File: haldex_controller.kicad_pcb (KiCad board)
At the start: 2 copper layers, 41 x 10.8 mm, 219 parts, among them IC1 TPS62A02DRLR, IC2 TPS2553DBVT, IC3 LBEE5KL1YN-814, IC4 TLIN1027DRQ1, J1 GND, J10 12V in, J11 K Line, J12 Brake Light, J13 Handbrake, J2 BOOT0, J3 JTAG, J4 Debug, J5 USB, J6 Conn_Coaxial_Small, J7 Body 120R, J8 Hldx 120R, J9 ECU Connector, Q1 STR1550, Q2 BC807, Q3 Si7119DN, SW1 ~{RST}, SW2 Config, U1 LMR33630BDDA, U10 G3VM-61VY2, U11 G3VM-61VY2, U12 G3VM-61VY2, U13 G3VM-61VY2, U14 G3VM-61VY2, U15 G3VM-61VY2, U16 G3VM-61VY2, U17 G3VM-61VY2, U2 STM32H573VITx, U3 PCA9557PW, U4 SST25VF080B-50-4x-S2Ax, U5 APS6404L-3SQR-SN, U6 USBLC6-2SC6, U8 TJA1051T-3, U9 TJA1051T-3, X1 32.768kHz, Y1 25MHz

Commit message: working on component placement
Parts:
- moved H3 265.3 mm to (158.8, 138.4)
- moved H2 261.5 mm to (157.5, 47.6)
- moved R4 258.1 mm to (159.7, 119.9)
- moved R3 255.1 mm to (155.9, 122.4)
- moved R5 254.7 mm to (160.0, 111.1)
- moved R6 253.8 mm to (160.0, 108.0), turned to 180 degrees
- moved R7 252.8 mm to (161.3, 84.7), turned to 90 degrees
- moved C9 252.1 mm to (156.2, 86.0)
- moved C2 252.0 mm to (156.2, 100.6)
- moved C7 251.7 mm to (156.2, 89.8)
- moved J10 249.7 mm to (158.1, 129.5), turned to 90 degrees
- moved R13 248.7 mm to (160.7, 97.4), turned to 90 degrees
- moved R12 248.5 mm to (160.7, 93.0), turned to 90 degrees
- moved Q2 245.8 mm to (154.8, 111.1)
- moved R8 243.5 mm to (149.9, 111.1), turned to -90 degrees
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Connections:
- D10 pad 1: GND -> Net-(D10-K)
- D10 pad 2: Net-(D10-A) -> /MCU/LED_HLDX_ERR
- D11 pad 1: GND -> Net-(D11-K)
- D11 pad 2: Net-(D11-A) -> /MCU/LED0
- D12 pad 1: GND -> Net-(D12-K)
- D12 pad 2: Net-(D12-A) -> /MCU/LED1
- D5 pad 1: GND -> Net-(D5-K)
- D5 pad 2: Net-(D5-A) -> /MCU/LED_BODY_TX
- D6 pad 1: GND -> Net-(D6-K)
- D6 pad 2: Net-(D6-A) -> /MCU/LED_BODY_RX
- D7 pad 1: GND -> Net-(D7-K)
- D7 pad 2: Net-(D7-A) -> /MCU/LED_BODY_ERR
- D8 pad 1: GND -> Net-(D8-K)
- D8 pad 2: Net-(D8-A) -> /MCU/LED_HLDX_TX
- D9 pad 1: GND -> Net-(D9-K)
- D9 pad 2: Net-(D9-A) -> /MCU/LED_HLDX_RX
- L7 pad 1: Net-(U8-CANH) -> Net-(U8-CANL)
- L7 pad 2: Net-(U8-CANL) -> /CAN PHYs/BODY_CAN_L
- L7 pad 4: /CAN PHYs/BODY_CAN_L -> Net-(U8-CANH)
- L8 pad 1: Net-(U9-CANH) -> Net-(U9-CANL)
- L8 pad 2: Net-(U9-CANL) -> /CAN PHYs/HLDX_CAN_L
- L8 pad 4: /CAN PHYs/HLDX_CAN_L -> Net-(U9-CANH)
- R30 pad 1: /MCU/LED_BODY_TX -> Net-(D5-K)
- R30 pad 2: Net-(D5-A) -> GND
- R31 pad 1: /MCU/LED_BODY_RX -> Net-(D6-K)
- R31 pad 2: Net-(D6-A) -> GND
- R32 pad 1: /MCU/LED_BODY_ERR -> Net-(D7-K)
- R32 pad 2: Net-(D7-A) -> GND
- R33 pad 1: /MCU/LED_HLDX_TX -> Net-(D8-K)
- R33 pad 2: Net-(D8-A) -> GND
- R34 pad 1: /MCU/LED_HLDX_RX -> Net-(D9-K)
- R34 pad 2: Net-(D9-A) -> GND
- R35 pad 1: /MCU/LED_HLDX_ERR -> Net-(D10-K)
- R35 pad 2: Net-(D10-A) -> GND
- R36 pad 1: /MCU/LED0 -> Net-(D11-K)
- R36 pad 2: Net-(D11-A) -> GND
- R37 pad 1: /MCU/LED1 -> Net-(D12-K)
- R37 pad 2: Net-(D12-A) -> GND
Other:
- board size 41 x 10.8 mm -> 68 x 100 mm
- copper layers 2 -> 4

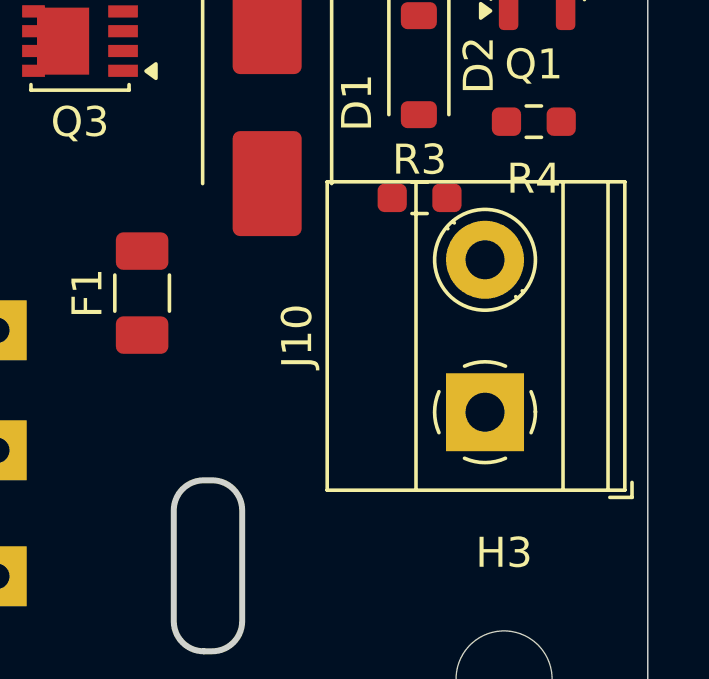
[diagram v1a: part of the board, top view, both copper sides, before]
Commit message: sch: J10 footprint update
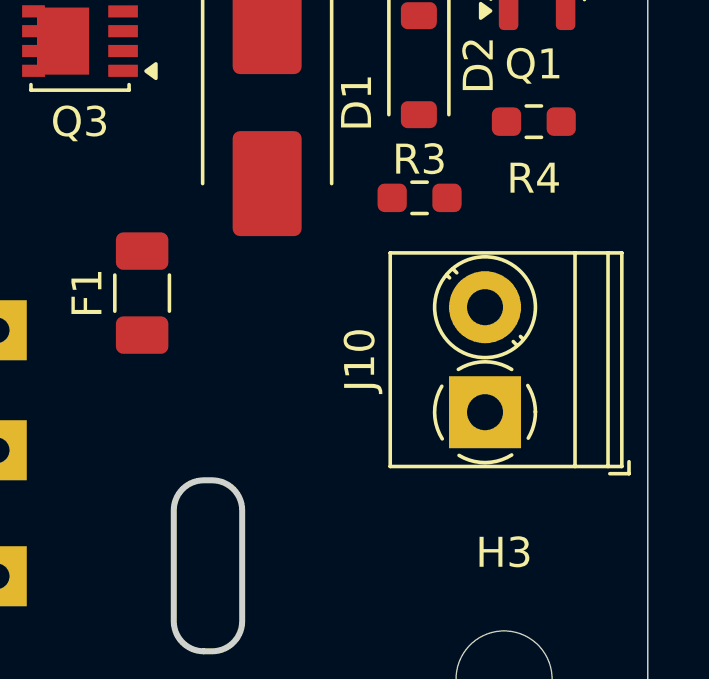
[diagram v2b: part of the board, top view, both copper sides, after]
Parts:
- J10: footprint TerminalBlock_Phoenix:TerminalBlock_Phoenix_MKDS-1,5-2-5.08_1x02_P5.08mm_Horizontal -> TerminalBlock_Phoenix:TerminalBlock_Phoenix_PT-1,5-2-3.5-H_1x02_P3.50mm_Horizontal

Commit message: brd: routing in progress
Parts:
- removed ANT1: W3000, W3000:W3000
- removed F2: 500mA, Fuse:Fuse_1206_3216Metric
- removed FB5, FB8: FerriteBead_Small, Inductor_SMD:L_0805_2012Metric_Pad1.05x1.20mm_HandSolder
- removed R48, R50: 0, Resistor_SMD:R_0402_1005Metric_Pad0.72x0.64mm_HandSolder
- removed TP10: SDIO_CMD, TestPoint:TestPoint_Pad_D1.0mm
- removed TP11: SDIO_DATA_2, TestPoint:TestPoint_Pad_D1.0mm
- removed TP12: SDIO_CLK, TestPoint:TestPoint_Pad_D1.0mm
- removed TP14: SDIO_DATA_0, TestPoint:TestPoint_Pad_D1.0mm
- removed TP15: SDIO_DATA_3, TestPoint:TestPoint_Pad_D1.0mm
- removed TP16: SDIO_DATA_1, TestPoint:TestPoint_Pad_D1.0mm
- added AE1: type1YN-antenna-p2ml4452-1, 1yn_antenna:1YN_ANTENNA, F.Cu at (98.4, 52.4)
- added C48: 4p7, Capacitor_SMD:C_0402_1005Metric_Pad0.74x0.62mm_HandSolder, F.Cu at (99.1, 63.3)
- added C49: 4p7, Capacitor_SMD:C_0402_1005Metric_Pad0.74x0.62mm_HandSolder, F.Cu at (99.1, 57.8)
- added C50: 100n, Capacitor_SMD:C_0603_1608Metric_Pad1.08x0.95mm_HandSolder, F.Cu at (133.9, 87.8)
- added C51: 100n, Capacitor_SMD:C_0603_1608Metric_Pad1.08x0.95mm_HandSolder, B.Cu at (154.7, 106.4)
- added L9: LQW15AN2N4B00D, Inductor_SMD:L_0402_1005Metric, F.Cu at (98.5, 52.8)
- added TP3: V_{BUS}, TestPoint:TestPoint_Pad_D1.0mm, F.Cu at (128.7, 54.2)
- C11, C12, C24, C31, C35, C37, C38, C39, C40, C41, C42, C43, C44, C45, C46, C47, D13, D14, D16, D17, D18, D19, F3, IC4, L4, L7, L8, R14, R18, R20, R25, R26, R27, R28, R30, R31, R32, R33, R34, R35, R36, R37, R51, R52, R53, R54, R69, R70, R71, TP13, U3, U8, U9, X1, Y1: moved to B.Cu
- J2: footprint Connector_PinHeader_2.54mm:PinHeader_1x02_P2.54mm_Vertical -> Connector_PinHeader_1.27mm:PinHeader_1x02_P1.27mm_Vertical
- J6: value Conn_Coaxial_Small -> MM8130-2600RA2; footprint Connector_Coaxial:U.FL_Molex_MCRF_73412-0110_Vertical -> MM8130-2600RA2:MM81302600RA2
- R42, R43, R44, R45, R46: footprint Resistor_SMD:R_0603_1608Metric_Pad0.98x0.95mm_HandSolder -> Resistor_SMD:R_0402_1005Metric_Pad0.72x0.64mm_HandSolder
- U4: footprint Package_SO:SOIC-8_5.275x5.275mm_P1.27mm -> Package_SO:SOIC-8_3.9x4.9mm_P1.27mm
- moved D4 372.5 mm to (144.0, 111.9), turned to -90 degrees
- moved R14 369.1 mm to (141.0, 114.0)
- moved L4 353.5 mm to (161.2, 108.8), turned to 90 degrees
- moved R27 305.2 mm to (148.1, 64.9), turned to 90 degrees
- moved C24 297.0 mm to (143.9, 65.0)
- moved R26 293.5 mm to (136.5, 62.0)
- moved R25 289.8 mm to (136.5, 63.8)
- moved U3 289.2 mm to (143.9, 60.2)
- moved D12 288.1 mm to (159.6, 54.5), turned to 0 degrees
- moved D5 285.8 mm to (159.6, 64.9), turned to 0 degrees
- moved D6 285.8 mm to (159.6, 62.1), turned to 0 degrees
- moved D7 285.7 mm to (159.6, 59.2), turned to 0 degrees
- moved R54 285.2 mm to (113.3, 118.4), turned to 90 degrees
- moved D8 281.0 mm to (152.1, 65.0), turned to 0 degrees
- moved R53 280.9 mm to (109.7, 118.4), turned to -90 degrees
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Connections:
- C33 pad 2: SR_PVSS -> GND
- C34 pad 2: Net-(C34-Pad2) -> Net-(J6-OUT)
- C35 pad 2: SR_PVSS -> GND
- D10 pad 1: Net-(D10-K) -> GND
- D10 pad 2: /MCU/LED_HLDX_ERR -> Net-(D10-A)
- D11 pad 1: Net-(D11-K) -> GND
- D11 pad 2: /MCU/LED0 -> Net-(D11-A)
- D12 pad 1: Net-(D12-K) -> GND
- D12 pad 2: /MCU/LED1 -> Net-(D12-A)
- D20 pad 1: /Connector/USER_INPUT_1 -> /Connector/USER_INPUT_2
- D20 pad 2: /Connector/USER_INPUT_2 -> /Connector/USER_INPUT_1
- D21 pad 1: /Connector/USER_OUTPUT_1 -> /Connector/USER_OUTPUT_2
- D21 pad 2: /Connector/USER_OUTPUT_2 -> /Connector/USER_OUTPUT_1
- D5 pad 1: Net-(D5-K) -> GND
- D5 pad 2: /MCU/LED_BODY_TX -> Net-(D5-A)
- D6 pad 1: Net-(D6-K) -> GND
- D6 pad 2: /MCU/LED_BODY_RX -> Net-(D6-A)
- D7 pad 1: Net-(D7-K) -> GND
- D7 pad 2: /MCU/LED_BODY_ERR -> Net-(D7-A)
- D8 pad 1: Net-(D8-K) -> GND
- D8 pad 2: /MCU/LED_HLDX_TX -> Net-(D8-A)
- D9 pad 1: Net-(D9-K) -> GND
- D9 pad 2: /MCU/LED_HLDX_RX -> Net-(D9-A)
- IC3 pad 32: SR_PVSS -> GND
- IC3 pad 33: SR_PVSS -> GND
- J5 pad A4: Net-(F2-Pad1) -> VBUS
- J5 pad A6: Net-(J5-D+-PadA6) -> /USB/USB_CONN_DP
- J5 pad A7: Net-(J5-D--PadA7) -> /USB/USB_CONN_DN
- J5 pad A9: Net-(F2-Pad1) -> VBUS
- J5 pad B4: Net-(F2-Pad1) -> VBUS
- J5 pad B6: Net-(J5-D+-PadA6) -> /USB/USB_CONN_DP
- J5 pad B7: Net-(J5-D--PadA7) -> /USB/USB_CONN_DN
- J5 pad B9: Net-(F2-Pad1) -> VBUS
- J6 pad 1: Net-(J6-In) -> /WiFi and Bluetooth/ANT_FEED
- J6 pad 2: GND -> Net-(J6-OUT)
- L5 pad 3: /MCU/USB_DN -> /MCU/USB_DP
- L5 pad 4: /MCU/USB_DP -> /MCU/USB_DN
- R30 pad 1: Net-(D5-K) -> /MCU/LED_BODY_TX
- R30 pad 2: GND -> Net-(D5-A)
- R31 pad 1: Net-(D6-K) -> /MCU/LED_BODY_RX
- R31 pad 2: GND -> Net-(D6-A)
- R32 pad 1: Net-(D7-K) -> /MCU/LED_BODY_ERR
- R32 pad 2: GND -> Net-(D7-A)
- R33 pad 1: Net-(D8-K) -> /MCU/LED_HLDX_TX
- R33 pad 2: GND -> Net-(D8-A)
- R34 pad 1: Net-(D9-K) -> /MCU/LED_HLDX_RX
- R34 pad 2: GND -> Net-(D9-A)
- R35 pad 1: Net-(D10-K) -> /MCU/LED_HLDX_ERR
- R35 pad 2: GND -> Net-(D10-A)
- R36 pad 1: Net-(D11-K) -> /MCU/LED0
- R36 pad 2: GND -> Net-(D11-A)
- R37 pad 1: Net-(D12-K) -> /MCU/LED1
- R37 pad 2: GND -> Net-(D12-A)
- R47 pad 1: /WiFi and Bluetooth/ANT_FEED -> Net-(C49-Pad2)
- R47 pad 2: Net-(J6-In) -> Net-(C36-Pad2)
- R49 pad 2: Net-(C34-Pad2) -> Net-(J6-OUT)
- U2 pad 2: unconnected-(U2-PE3-Pad2) -> /CAN PHYs/HLDX_CAN_S
- U2 pad 61: /MCU/DIP_3 -> /MCU/DIP_4
- U2 pad 62: /MCU/DIP_4 -> /MCU/DIP_3
- U2 pad 93: /CAN PHYs/HLDX_CAN_S -> unconnected-(U2-PB7-Pad93)
- U3 pad 10: /MCU/LED_HLDX_TX -> /MCU/LED_HLDX_ERR
- U3 pad 11: /MCU/LED_HLDX_RX -> /MCU/LED_BODY_RX
- U3 pad 12: /MCU/LED_HLDX_ERR -> /MCU/LED_HLDX_RX
- U3 pad 13: /MCU/LED0 -> /MCU/LED_BODY_TX
- U3 pad 14: /MCU/LED1 -> /MCU/LED_HLDX_TX
- U3 pad 6: /MCU/LED_BODY_TX -> /MCU/LED1
- U3 pad 7: /MCU/LED_BODY_RX -> /MCU/LED0
- U6 pad 1: Net-(J5-D--PadA7) -> /USB/USB_CONN_DP
- U6 pad 3: Net-(J5-D+-PadA6) -> /USB/USB_CONN_DN
- U6 pad 5: Net-(U6-VBUS) -> VBUS
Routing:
- net +3V3: track 0.00 -> 89.9 mm, vias 0 -> 17
- net /MCU/MCU_USER_INPUT_1: track 0.00 -> 87.4 mm, vias 0 -> 2
- net /MCU/MCU_BODY_HANDBRAKE: track 0.00 -> 86.0 mm, vias 0 -> 2
- net /MCU/MCU_BODY_BRAKES: track 0.00 -> 83.6 mm, vias 0 -> 2
- net /MCU/MCU_USER_INPUT_2: track 0.00 -> 80.8 mm, vias 0 -> 2
- net /Connector/HLDX_K_LINE: track 0.00 -> 72.5 mm
- net /Connector/USER_INPUT_2: track 0.00 -> 67.9 mm
- net /CAN PHYs/BODY_CAN_S: track 0.00 -> 62.4 mm, vias 0 -> 1
- net /Connector/USER_INPUT_1: track 0.00 -> 62.3 mm
- net /MCU/I2S2_WS: track 0.00 -> 62.0 mm, vias 0 -> 2
- net /MCU/MCU_HLDX_HANDBRAKE: track 0.00 -> 61.3 mm, vias 0 -> 2
- net /MCU/LIN_EN: track 0.00 -> 60.0 mm, vias 0 -> 1
- net /MCU/MCU_HLDX_BRAKES: track 0.00 -> 59.5 mm, vias 0 -> 2
- net /MCU/LIN_TX: track 0.00 -> 58.4 mm, vias 0 -> 1
- net /MCU/JTAG_~{RST}: track 0.00 -> 58.4 mm, vias 0 -> 3
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- added copper zone on F.Cu, net +3V3
- added copper zone on B.Cu, net +BATT
- added copper zone on F.Cu, net +BATT
- added copper zone on B.Cu, net /Connector/USER_BATT
- added copper zone on F.Cu, net /WiFi and Bluetooth/SR_VLX
- added copper zone on F.Cu, net /WiFi and Bluetooth/VIN_LDO
- added copper zone on B.Cu, net GND
- added copper zone on F.Cu, net GND
- added copper zone on In1.Cu, net GND
- added copper zone on B.Cu, net GNDPWR
- added copper zone on F.Cu, net GNDPWR
- added copper zone on F.Cu, net Net-(C10-Pad2)
- added copper zone on F.Cu, net Net-(D1-A)
- added copper zone on F.Cu, net Net-(D1-K)
- added copper zone on F.Cu, net Net-(Q3-D)
- added copper zone on F.Cu, net Net-(U1-EN)
- added copper zone on F.Cu, net Net-(U1-SW)
- added copper zone on F.Cu, net VCC
- added copper zone on B.Cu, net VIO
- added copper zone on F.Cu, net VIO
- added copper zone on In2.Cu, net VIO
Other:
- outline, holes or cut-outs redrawn
- board text added: "BODY"
- board text added: "BOOT0"
- board text added: "ERR"
- board text added: "GND"
- board text added: "HLDX"
- board text added: "JLCJLCJLCJLC"
- board text added: "LED0"
- board text added: "LED1"
- board text added: "RST"
- board text added: "RX"
- board text added: "TX"

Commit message: brd: layout complete
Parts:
- removed C28, C30: 100n, Capacitor_SMD:C_0603_1608Metric_Pad1.08x0.95mm_HandSolder
- removed C29: 10u, Capacitor_SMD:C_0603_1608Metric_Pad1.08x0.95mm_HandSolder
- removed FB6: FerriteBead_Small, Inductor_SMD:L_0805_2012Metric_Pad1.05x1.20mm_HandSolder
- removed IC2: TPS2553DBVT, TPS2553DBVT:SOT95P280X145-6N
- removed J11: K Line, Connector_PinHeader_2.54mm:PinHeader_1x02_P2.54mm_Horizontal
- removed J12: Brake Light, Connector_PinHeader_2.54mm:PinHeader_1x02_P2.54mm_Horizontal
- removed J13: Handbrake, Connector_PinHeader_2.54mm:PinHeader_1x02_P2.54mm_Horizontal
- removed R40: 100k, Resistor_SMD:R_0603_1608Metric_Pad0.98x0.95mm_HandSolder
- removed R41: 55k, Resistor_SMD:R_0603_1608Metric_Pad0.98x0.95mm_HandSolder
- removed TP6: ~{FAULT}, TestPoint:TestPoint_Pad_D1.5mm
- removed TP7: nRF V_{DDIO}, TestPoint:TestPoint_Pad_D1.5mm
- removed TP8: nRF7002 BUCK EN, TestPoint:TestPoint_Pad_D1.5mm
- removed TP9: nRF7002 IRQ, TestPoint:TestPoint_Pad_D1.5mm
- removed U7: ~, ptr7002:ptr7002
- added J15: nRF7002 Ext, Connector_PinHeader_1.27mm:PinHeader_2x05_P1.27mm_Vertical, F.Cu at (159.8, 70.2)
- added JP1: K Line, Jumper:SolderJumper-2_P1.3mm_Open_TrianglePad1.0x1.5mm, B.Cu at (99.8, 122.0)
- added JP2: Brake Light, Jumper:SolderJumper-2_P1.3mm_Open_TrianglePad1.0x1.5mm, B.Cu at (99.8, 126.0)
- added JP3: Handbrake, Jumper:SolderJumper-2_P1.3mm_Open_TrianglePad1.0x1.5mm, B.Cu at (99.9, 129.9)
- added REF**: KiCad-Logo2_5mm_SilkScreen, Symbol:KiCad-Logo2_5mm_SilkScreen, B.Cu at (110.6, 59.3)
- FB7: moved to B.Cu
- moved R15 188.9 mm to (140.6, 93.1), turned to 180 degrees
- moved R16 185.9 mm to (137.9, 87.2), turned to 90 degrees
- moved C13 180.4 mm to (137.0, 91.2), turned to -90 degrees
- moved C27 66.3 mm to (145.3, 83.3), turned to -90 degrees
- moved FB7 20.7 mm to (99.2, 80.8)
- moved R7 4.36 mm to (159.1, 88.5), turned to 0 degrees
- moved TP2 4.01 mm to (159.3, 85.1), turned to 0 degrees
- moved FB3 3.74 mm to (148.7, 86.0), turned to 180 degrees
- moved U5 2.86 mm to (152.1, 74.0)
- moved L4 2.29 mm to (161.0, 106.6)
- moved C9 2.04 mm to (154.2, 85.9)
- moved C7 2.03 mm to (154.2, 89.8)
- moved D4 1.53 mm to (143.0, 110.7)
- moved C51 1.45 mm to (153.3, 106.2), turned to -90 degrees
- moved C26 0.45 mm to (155.4, 69.2), turned to 180 degrees
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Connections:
- C27 pad 1: VDD_nRF -> +3V3
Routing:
- net GNDPWR: track 0.00 -> 189.7 mm, vias 0 -> 8
- net +5V: track 5.40 -> 88.8 mm, vias 0 -> 6
- net +BATT: track 0.00 -> 54.9 mm, vias 0 -> 3
- net /Connector/HLDX_BRAKE_LIGHT_SWITCH: track 38.2 -> 87.9 mm, vias 1 -> 2
- net /Connector/HLDX_K_LINE: track 72.5 -> 115.5 mm, vias 0 -> 1
- net /Connector/HLDX_HANDBRAKE: track 33.1 -> 72.2 mm, vias 1 -> 2
- net VCC: track 0.00 -> 37.9 mm, vias 0 -> 2
- net /Connector/BODY_K_LINE: track 3.51 -> 37.4 mm, vias 0 -> 1
- net +3V3: track 89.9 -> 122.0 mm, vias 17 -> 31
- net /MCU/SPI1_~{CS}: track 0.00 -> 29.5 mm, vias 0 -> 1
- net /MCU/nRF7002_BUCK_EN: track 0.00 -> 27.3 mm, vias 0 -> 1
- net /MCU/nRF7002_VDDIO_EN: track 0.00 -> 24.8 mm, vias 0 -> 1
- net /MCU/SPI1_MOSI: track 0.00 -> 20.6 mm
- net /MCU/SPI1_MISO: track 0.00 -> 19.9 mm
- net /MCU/nRF7002_IRQ: track 0.00 -> 19.8 mm, vias 0 -> 1
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- added copper zone on B.Cu, net +3V3
- added copper zone on In2.Cu, net +3V3
- added copper zone on F.Cu, net Net-(C7-Pad1)
- added copper zone on F.Cu, net Net-(IC1-EN)
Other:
- outline, holes or cut-outs redrawn
- board text added: "120R"
- board text added: "12V"
- board text added: "Brake"
- board text added: "GrippyBoi"
- board text added: "HBrake"
- board text added: "K Line"
- board text added: "github.com/gabbla/grippyboi"

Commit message: brd: add version
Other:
- board text added: "v1.0.0"
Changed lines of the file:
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@@
+		)
+	)
+	(gr_text "v1.0.0"
+		(at 110.49 65.786 0)
+		(layer "F.SilkS")
+		(effects
+			(font
+				(size 0.7 0.7)
+				(thickness 0.1)
+			)
+			(justify left bottom)
 		)
 	)
@@
 	)
 	(gr_text "github.com/gabbla/grippyboi"
-		(at 104.394 59.309 0)
+		(at 104.394 59.563 0)
 		(layer "F.SilkS")
 		(effects
